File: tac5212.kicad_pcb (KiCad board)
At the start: 4 copper layers, 43.2 x 35.6 mm, 49 parts, among them J1 DIGI, J2 AIN, J3 AOUT, J4 DIN, J5 VDC, J6 Qwiic, J8 CLK, U1 XTAC5212IRGER, U2 SPX3819M5-L-3-3, Y1 830207659209

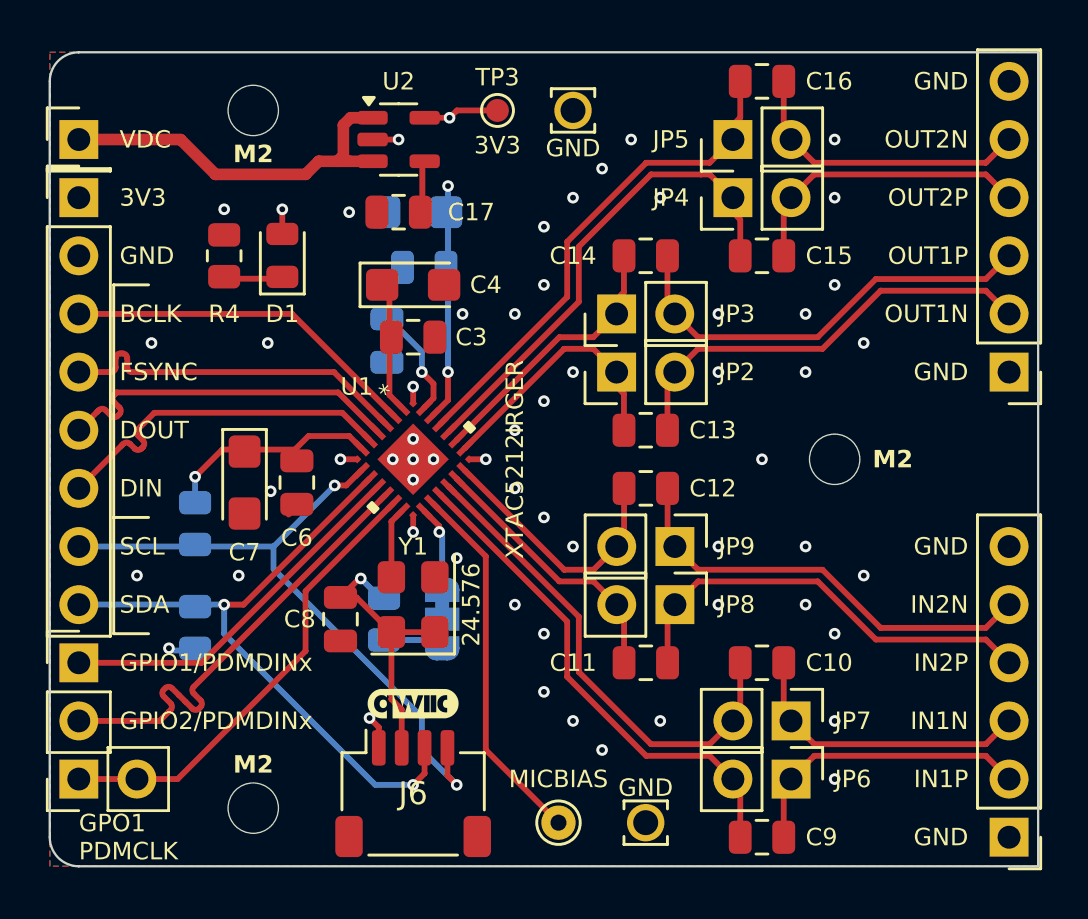
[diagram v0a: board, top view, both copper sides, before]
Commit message: v1.0 sent to fab - added AVDD supply
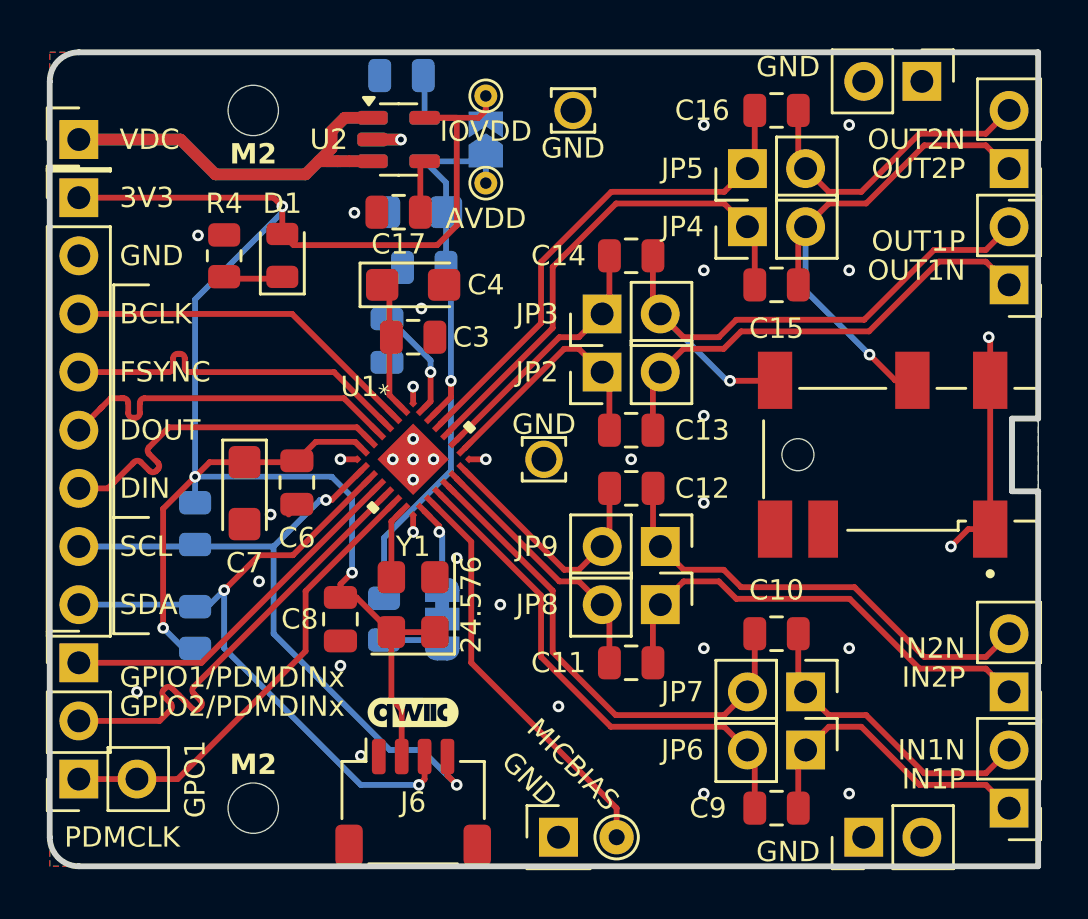
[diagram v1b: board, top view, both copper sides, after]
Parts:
- removed H1: MH, MountingHole:MountingHole_2.2mm_M2
- added C18: 0.1uF, Capacitor_SMD:C_0805_2012Metric, B.Cu at (96.6, 51.8)
- added J10: AIN_GND, Connector_PinHeader_2.54mm:PinHeader_1x02_P2.54mm_Vertical, F.Cu at (116.8, 85.1)
- added J11: AOUT1, Connector_PinHeader_2.54mm:PinHeader_1x02_P2.54mm_Vertical, F.Cu at (123.2, 61.0)
- added J12: AOUT2, Connector_PinHeader_2.54mm:PinHeader_1x02_P2.54mm_Vertical, F.Cu at (123.2, 55.9)
- added J13: 54-00178, Headphone_Jack:TENSILITY_54-00178, F.Cu at (118.5, 68.6)
- added J7: MIC_GND, Connector_PinHeader_2.54mm:PinHeader_1x01_P2.54mm_Vertical, F.Cu at (103.5, 85.1)
- added J9: AIN2, Connector_PinHeader_2.54mm:PinHeader_1x02_P2.54mm_Vertical, F.Cu at (123.2, 78.7)
- added JP10: Jumper_2_Small_Open, Jumper:SolderJumper-2_P1.3mm_Open_TrianglePad1.0x1.5mm, B.Cu at (100.3, 54.6)
- added TP5: AVDD, TestPoint:TestPoint_THTPad_D1.0mm_Drill0.5mm, F.Cu at (100.3, 56.5)
- added U3: SPX3819M5-L-3-3, Package_TO_SOT_SMD:SOT-23-5, B.Cu at (96.5, 54.6)
- J2: value AIN -> AIN1; footprint Connector_PinHeader_2.54mm:PinHeader_1x06_P2.54mm_Vertical -> Connector_PinHeader_2.54mm:PinHeader_1x02_P2.54mm_Vertical
- J3: value AOUT -> AOUT_GND; footprint Connector_PinHeader_2.54mm:PinHeader_1x06_P2.54mm_Vertical -> Connector_PinHeader_2.54mm:PinHeader_1x02_P2.54mm_Vertical
- TP3: value 3V3 -> IOVDD; footprint TestPoint:TestPoint_Pad_D1.0mm -> TestPoint:TestPoint_THTPad_D1.0mm_Drill0.5mm
- moved TP2 16.5 mm to (102.9, 68.6)
- moved J3 13.3 mm to (119.4, 52.1), turned to -90 degrees
- moved TP1 2.62 mm to (106.0, 85.1)
- moved C9 1.42 mm to (113.0, 83.8)
- moved C15 1.42 mm to (113.0, 61.0)
- moved C16 1.42 mm to (113.0, 53.3)
- moved JP4 1.42 mm to (111.8, 58.4)
- moved JP5 1.42 mm to (111.8, 55.9)
- moved JP7 1.42 mm to (114.3, 78.7)
- moved C10 1.42 mm to (113.0, 76.2)
- moved JP6 1.42 mm to (114.3, 81.3)
- moved J2 1.27 mm to (123.2, 83.8)
- moved TP3 0.81 mm to (100.3, 52.7)
- moved C11 0.64 mm to (106.7, 77.5)
- moved JP2 0.64 mm to (105.4, 64.8)
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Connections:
- C1 pad 1: +3.3V -> AVDD
- C2 pad 1: +3.3V -> AVDD
- J2 pad 1: GND -> /CIN1P
- J2 pad 2: /CIN1P -> /CIN1N
- J3 pad 2: /COUT1N -> GND
- R1 pad 1: +3.3V -> AVDD
- U1 pad 23: +3.3V -> AVDD
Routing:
- net +3.3V: track 37.8 -> 82.6 mm, vias 7 -> 4
- net AVDD: track 0.00 -> 26.7 mm, vias 0 -> 1
- net VDC: track 16.8 -> 35.3 mm
- net GND: track 6.05 -> 17.1 mm, vias 56 -> 34
- net /COUT2P: track 13.0 -> 22.5 mm, vias 0 -> 1
- net /COUT1P: track 19.2 -> 26.7 mm, vias 0 -> 1
- net Net-(U3-BP): track 0.00 -> 1.87 mm
- net Net-(U1A-MICBIAS): track 16.3 -> 17.9 mm
- net /CIN2P: track 19.2 -> 20.3 mm
- net /CIN2N: track 19.2 -> 20.3 mm
- net /COUT1N: track 19.2 -> 20.3 mm
- net SDA: track 29.1 -> 30.2 mm
- net SCL: track 29.2 -> 30.1 mm
- net /IN2P: track 11.9 -> 11.3 mm
- net /IN2N: track 11.5 -> 10.9 mm
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- added copper zone on In2.Cu, net GND
- removed copper zone on In2.Cu, net +3.3V
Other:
- outline, holes or cut-outs redrawn
- board text added: "GPO1"
- board text added: "PDMCLK"
- board text added: "Slot cutout"
- board text removed: "GPO1 PDMCLK"
